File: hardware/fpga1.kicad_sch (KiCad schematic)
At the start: 2 parts

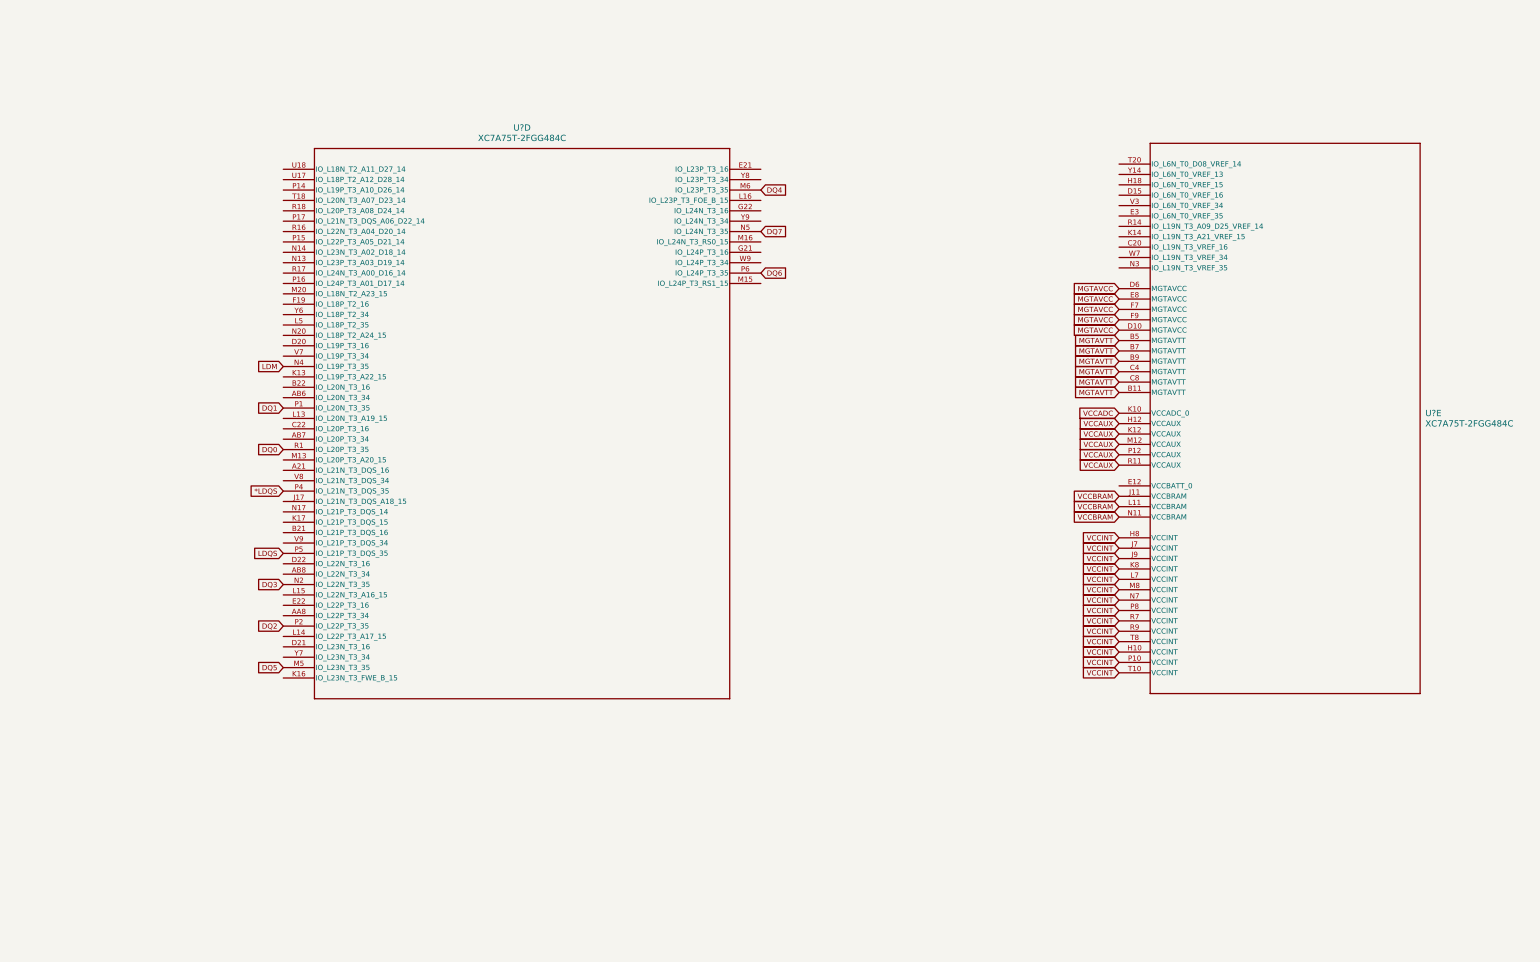
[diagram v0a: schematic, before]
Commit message: finished schematic!!! :D (before peer review)
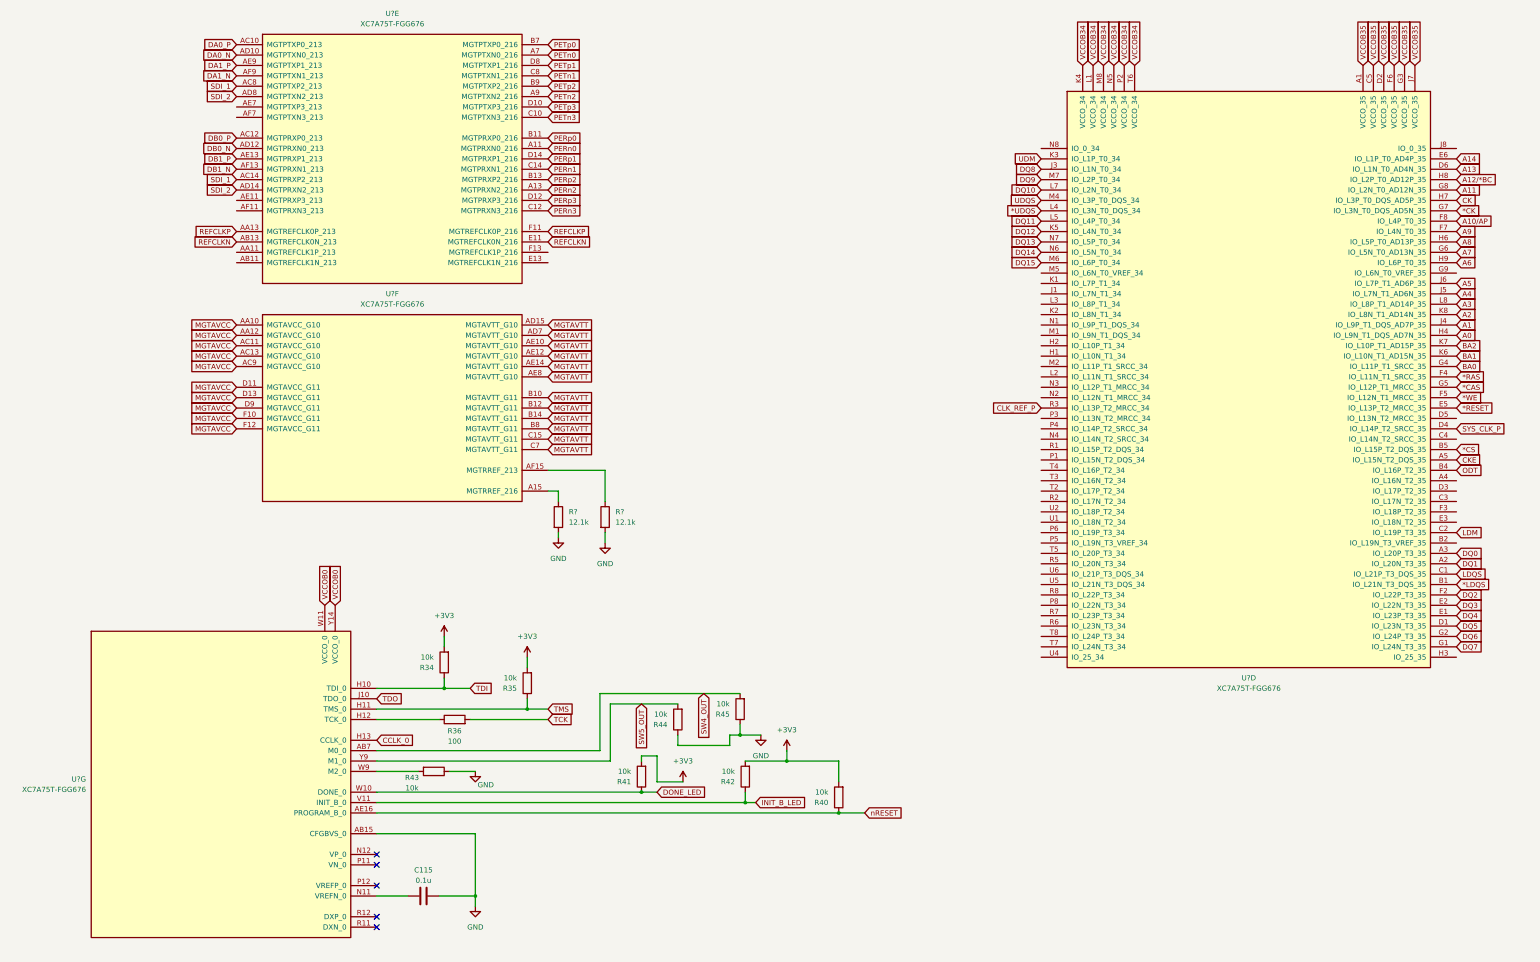
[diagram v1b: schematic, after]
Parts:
- removed U? (x2): XC7A75T-2FGG484C, FGG484ARTIX-7_AMD, symbol arcticvideo:XC7A75T-2FGG484C
- added C115: 0.1u, symbol Device:C
- added R34, R35, R40, R41, R42, R43, R44, R45: 10k, symbol Device:R
- added R36: 100, symbol Device:R
- added R? (x2): 12.1k, symbol Device:R
- added U? (x4): XC7A75T-FGG676, symbol FPGA_Xilinx_Artix7:XC7A75T-FGG676
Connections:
- net *LDQS: now also U?.B1 (IO_L21N_T3_DQS_35)
- net DQ0: now also U?.A3 (IO_L20P_T3_35)
- net DQ1: now also U?.A2 (IO_L20N_T3_35)
- net DQ2: now also U?.F2 (IO_L22P_T3_35)
- net DQ3: now also U?.E2 (IO_L22N_T3_35)
- net DQ4: now also U?.E1 (IO_L23P_T3_35)
- net DQ5: now also U?.D1 (IO_L23N_T3_35)
- net DQ6: now also U?.G2 (IO_L24P_T3_35)
- net DQ7: now also U?.G1 (IO_L24N_T3_35)
- net LDM: now also U?.C2 (IO_L19P_T3_35)
- net LDQS: now also U?.C1 (IO_L21P_T3_DQS_35)
- net MGTAVCC: now also U?.AA10 (MGTAVCC_G10), U?.AA12 (MGTAVCC_G10), U?.AC11 (MGTAVCC_G10), U?.AC13 (MGTAVCC_G10), U?.AC9 (MGTAVCC_G10), U?.D11 (MGTAVCC_G11), U?.D13 (MGTAVCC_G11), U?.D9 (MGTAVCC_G11), U?.F10 (MGTAVCC_G11), U?.F12 (MGTAVCC_G11)
- net MGTAVTT: now also U?.AD15 (MGTAVTT_G10), U?.AD7 (MGTAVTT_G10), U?.AE10 (MGTAVTT_G10), U?.AE12 (MGTAVTT_G10), U?.AE14 (MGTAVTT_G10), U?.AE8 (MGTAVTT_G10), U?.B10 (MGTAVTT_G11), U?.B12 (MGTAVTT_G11), U?.B14 (MGTAVTT_G11), U?.B8 (MGTAVTT_G11), U?.C15 (MGTAVTT_G11), U?.C7 (MGTAVTT_G11)
- new net: R36.1, U?.H12 (TCK_0)
- new net: C115.1, U?.N11 (VREFN_0)
- new net: R43.2, U?.W9 (M2_0)
- new net: R?.1, U?.A15 (MGTRREF_216)
- new net: R?.1, U?.AF15 (MGTRREF_213)
- new net *CAS: U?.G5 (IO_L12P_T1_MRCC_35)
- new net *CK: U?.G7 (IO_L3N_T0_DQS_AD5N_35)
- new net *CS: U?.B5 (IO_L15P_T2_DQS_35)
- new net *RAS: U?.F4 (IO_L11N_T1_SRCC_35)
- new net *RESET: U?.E5 (IO_L13P_T2_MRCC_35)
- new net *UDQS: U?.L4 (IO_L3N_T0_DQS_34)
- new net *WE: U?.F5 (IO_L12N_T1_MRCC_35)
- new net +3V3: R34.2, R35.2, R40.2, R41.2, R42.2
- new net A0: U?.H4 (IO_L9N_T1_DQS_AD7N_35)
- new net A1: U?.J4 (IO_L9P_T1_DQS_AD7P_35)
- new net A10/AP: U?.F8 (IO_L4P_T0_35)
- new net A11: U?.G8 (IO_L2N_T0_AD12N_35)
- new net A12/*BC: U?.H8 (IO_L2P_T0_AD12P_35)
- new net A13: U?.D6 (IO_L1N_T0_AD4N_35)
- new net A14: U?.E6 (IO_L1P_T0_AD4P_35)
- new net A2: U?.K8 (IO_L8N_T1_AD14N_35)
- new net A3: U?.L8 (IO_L8P_T1_AD14P_35)
- new net A4: U?.J5 (IO_L7N_T1_AD6N_35)
- new net A5: U?.J6 (IO_L7P_T1_AD6P_35)
- new net A6: U?.H9 (IO_L6P_T0_35)
- new net A7: U?.G6 (IO_L5N_T0_AD13N_35)
- new net A8: U?.H6 (IO_L5P_T0_AD13P_35)
- new net A9: U?.F7 (IO_L4N_T0_35)
- new net BA0: U?.G4 (IO_L11P_T1_SRCC_35)
- new net BA1: U?.K6 (IO_L10N_T1_AD15N_35)
- new net BA2: U?.K7 (IO_L10P_T1_AD15P_35)
- new net CCLK_0: U?.H13 (CCLK_0)
- new net CK: U?.H7 (IO_L3P_T0_DQS_AD5P_35)
- new net CKE: U?.A5 (IO_L15N_T2_DQS_35)
- new net CLK_REF_P: U?.R3 (IO_L13P_T2_MRCC_34)
- new net DA0_N: U?.AD10 (MGTPTXN0_213)
- new net DA0_P: U?.AC10 (MGTPTXP0_213)
- new net DA1_N: U?.AF9 (MGTPTXN1_213)
- new net DA1_P: U?.AE9 (MGTPTXP1_213)
- new net DB0_N: U?.AD12 (MGTPRXN0_213)
- new net DB0_P: U?.AC12 (MGTPRXP0_213)
- new net DB1_N: U?.AF13 (MGTPRXN1_213)
- new net DB1_P: U?.AE13 (MGTPRXP1_213)
- new net DONE_LED: R41.1, U?.W10 (DONE_0)
- new net DQ10: U?.L7 (IO_L2N_T0_34)
- new net DQ11: U?.L5 (IO_L4P_T0_34)
- new net DQ12: U?.K5 (IO_L4N_T0_34)
- new net DQ13: U?.N7 (IO_L5P_T0_34)
- new net DQ14: U?.N6 (IO_L5N_T0_34)
- new net DQ15: U?.M6 (IO_L6P_T0_34)
- new net DQ8: U?.J3 (IO_L1N_T0_34)
- new net DQ9: U?.M7 (IO_L2P_T0_34)
- new net GND: C115.2, R43.1, R44.1, R45.1, R?.2, R?.2, U?.AB15 (CFGBVS_0)
- new net INIT_B_LED: R42.1, U?.V11 (INIT_B_0)
- new net ODT: U?.B4 (IO_L16P_T2_35)
- new net PERn0: U?.A11 (MGTPRXN0_216)
- new net PERn1: U?.C14 (MGTPRXN1_216)
- new net PERn2: U?.A13 (MGTPRXN2_216)
- new net PERn3: U?.C12 (MGTPRXN3_216)
- new net PERp0: U?.B11 (MGTPRXP0_216)
- new net PERp1: U?.D14 (MGTPRXP1_216)
- new net PERp2: U?.B13 (MGTPRXP2_216)
- new net PERp3: U?.D12 (MGTPRXP3_216)
- new net PETn0: U?.A7 (MGTPTXN0_216)
- new net PETn1: U?.C8 (MGTPTXN1_216)
- new net PETn2: U?.A9 (MGTPTXN2_216)
- new net PETn3: U?.C10 (MGTPTXN3_216)
- new net PETp0: U?.B7 (MGTPTXP0_216)
- new net PETp1: U?.D8 (MGTPTXP1_216)
- new net PETp2: U?.B9 (MGTPTXP2_216)
- new net PETp3: U?.D10 (MGTPTXP3_216)
- new net REFCLKN: U?.AB13 (MGTREFCLK0N_213), U?.E11 (MGTREFCLK0N_216)
- new net REFCLKP: U?.AA13 (MGTREFCLK0P_213), U?.F11 (MGTREFCLK0P_216)
- new net SDI_1: U?.AC14 (MGTPRXP2_213), U?.AC8 (MGTPTXP2_213)
- new net SDI_2: U?.AD14 (MGTPRXN2_213), U?.AD8 (MGTPTXN2_213)
- new net SW4_OUT: R45.2, U?.AB7 (M0_0)
- new net SW5_OUT: R44.2, U?.Y9 (M1_0)
- new net SYS_CLK_P: U?.D4 (IO_L14P_T2_SRCC_35)
- new net TCK: R36.2
- new net TDI: R34.1, U?.H10 (TDI_0)
- new net TDO: U?.J10 (TDO_0)
- new net TMS: R35.1, U?.H11 (TMS_0)
- new net UDM: U?.K3 (IO_L1P_T0_34)
- new net UDQS: U?.M4 (IO_L3P_T0_DQS_34)
- new net VCCOB0: U?.W11 (VCCO_0), U?.Y14 (VCCO_0)
- new net VCCOB34: U?.K4 (VCCO_34), U?.L1 (VCCO_34), U?.M8 (VCCO_34), U?.N5 (VCCO_34), U?.P2 (VCCO_34), U?.T6 (VCCO_34)
- new net VCCOB35: U?.A1 (VCCO_35), U?.C5 (VCCO_35), U?.D2 (VCCO_35), U?.F6 (VCCO_35), U?.G3 (VCCO_35), U?.J7 (VCCO_35)
- new net nRESET: R40.1, U?.AE16 (PROGRAM_B_0)
- no-connect marks 0 -> 5

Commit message: readable changes
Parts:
- removed R44, R45: 10k, symbol Device:R
- added R54, R56: 10k, symbol Device:R
- gave numbers to parts that had none: 4
- renumbered C115 to C134, R34 to R50, R43 to R51, R36 to R52, R35 to R53, R41 to R58, R42 to R59, R40 to R60
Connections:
- net GND: now also R54.2, R56.2
- net SW4_OUT: now also R54.1
- net SW5_OUT: now also R56.1
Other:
- moved on the sheet: R50, R51, R52, R53, R58, R59, R60

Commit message: pcb routing
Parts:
- removed U14: XC7A75T-FGG676, symbol FPGA_Xilinx_Artix7:XC7A75T-FGG676
- added unit 6 of U1
- C134: footprint (none) -> Capacitor_SMD:C_0402_1005Metric
- R48: renamed from R50; footprint (none) -> Resistor_SMD:R_0402_1005Metric
- R49: renamed from R51; footprint (none) -> Resistor_SMD:R_0402_1005Metric
- R50: renamed from R52; footprint (none) -> Resistor_SMD:R_0402_1005Metric
- R51: renamed from R53; footprint (none) -> Resistor_SMD:R_0402_1005Metric
- R52: renamed from R54; footprint (none) -> Resistor_SMD:R_0402_1005Metric
- R53: renamed from R55; footprint (none) -> Resistor_SMD:R_0402_1005Metric
- R54: renamed from R56; footprint (none) -> Resistor_SMD:R_0402_1005Metric
- R55: renamed from R57; footprint (none) -> Resistor_SMD:R_0402_1005Metric
- R56: renamed from R58; footprint (none) -> Resistor_SMD:R_0402_1005Metric
- R57: renamed from R59; footprint (none) -> Resistor_SMD:R_0402_1005Metric
- R58: renamed from R60; footprint (none) -> Resistor_SMD:R_0402_1005Metric
- U1: footprint (none) -> Package_BGA:Xilinx_FGG676
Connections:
- net MGTAVCC: now also U1.AA10 (MGTAVCC_G10), U1.AA12 (MGTAVCC_G10), U1.AC11 (MGTAVCC_G10), U1.AC13 (MGTAVCC_G10), U1.AC9 (MGTAVCC_G10), U1.D11 (MGTAVCC_G11), U1.D13 (MGTAVCC_G11), U1.D9 (MGTAVCC_G11), U1.F10 (MGTAVCC_G11), U1.F12 (MGTAVCC_G11)
- net MGTAVTT: now also U1.AD15 (MGTAVTT_G10), U1.AD7 (MGTAVTT_G10), U1.AE10 (MGTAVTT_G10), U1.AE12 (MGTAVTT_G10), U1.AE14 (MGTAVTT_G10), U1.AE8 (MGTAVTT_G10), U1.B10 (MGTAVTT_G11), U1.B12 (MGTAVTT_G11), U1.B14 (MGTAVTT_G11), U1.B8 (MGTAVTT_G11), U1.C15 (MGTAVTT_G11), U1.C7 (MGTAVTT_G11)
- net at R53.1: now also U1.A15 (MGTRREF_216)
- net at R55.1: now also U1.AF15 (MGTRREF_213)
